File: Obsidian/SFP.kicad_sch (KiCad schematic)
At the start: 41 parts, among them J1 TYCO_1888247-1, J12 TYCO_1888247-1, J8 2180739-1, U17 TCA9555RTWR, U26 PCA9546ARGV

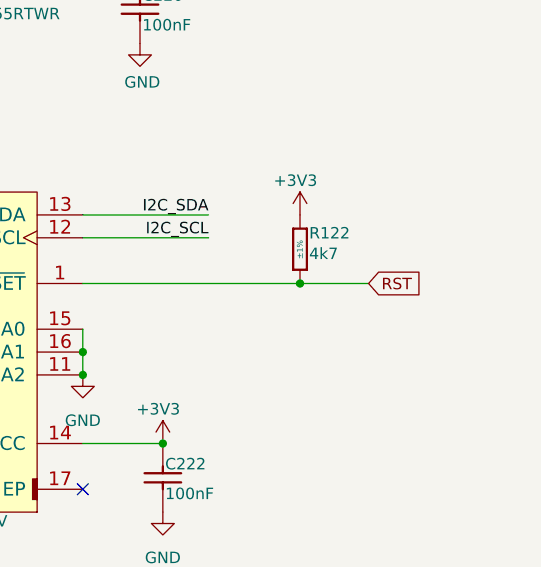
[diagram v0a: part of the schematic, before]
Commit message: removing reset global label
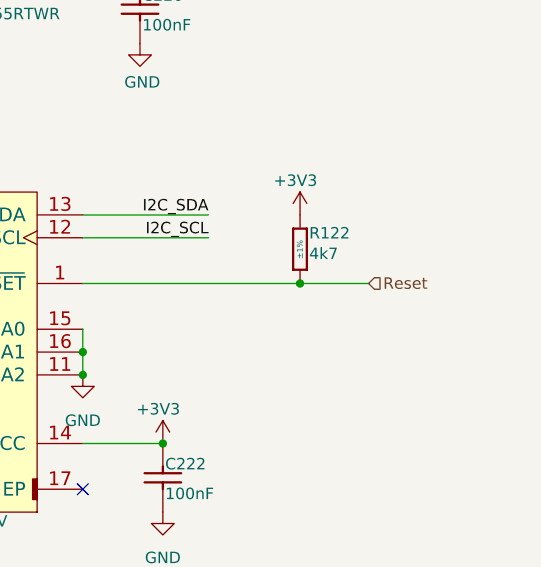
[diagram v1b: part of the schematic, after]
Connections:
- net RST renamed Reset
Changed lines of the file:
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@@
 		)
 	)
-	(global_label "RST"
+	(hierarchical_label "Reset"
 		(shape input)
 		(at 378.46 111.76 0)
-		(fields_autoplaced yes)
 		(effects
 			(font
@@
 			(justify left)
 		)
-		(property "Intersheetrefs" "${INTERSHEET_REFS}"
-			(at 384.8923 111.76 0)
-			(effects
-				(font
-					(size 1.27 1.27)
-				)
-				(justify left)
-				(hide yes)
-			)
-		)
 	)

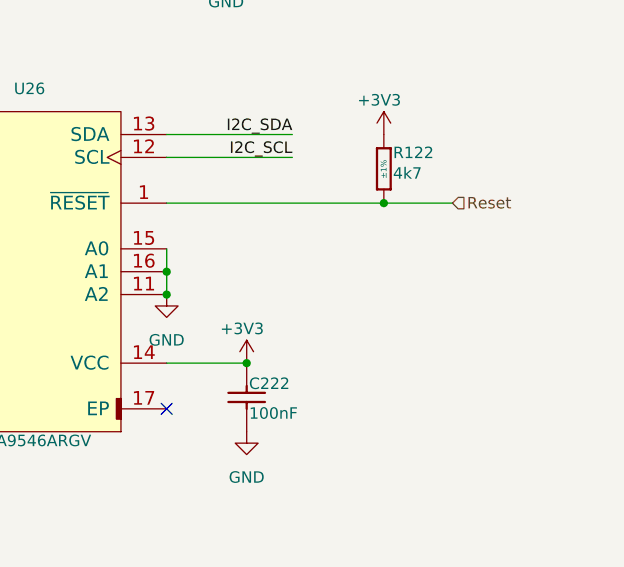
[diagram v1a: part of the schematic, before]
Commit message: adding lcsc reference for PMOD
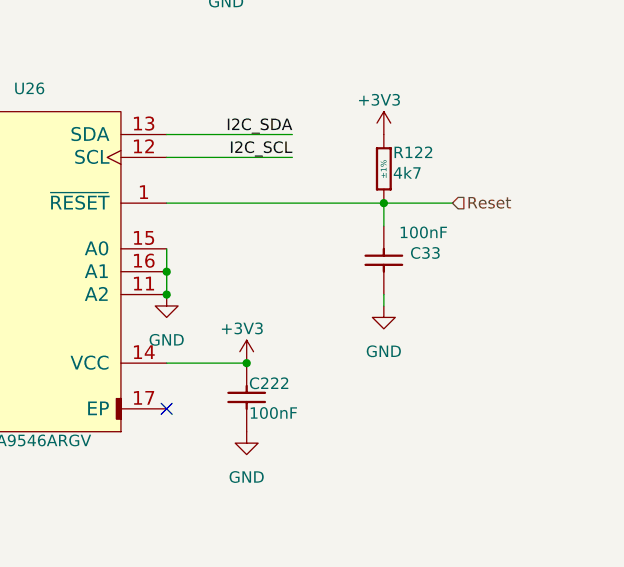
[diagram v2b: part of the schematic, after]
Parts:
- added C33: CC0402_100NF_50V_10%_X7R, Capacitor_SMD:C_0402_1005Metric, symbol Library_Symbol:CC0402_100NF_50V_10%_X7R
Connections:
- net GND: now also C33.2
- net Reset: now also C33.1

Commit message: update LCSC reference, and OFFSET rotation for JLCPCB
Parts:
- C20, C21, C22, C220, C222, C24, C25, C26, C29, C30, C33: footprint Capacitor_SMD:C_0402_1005Metric -> Footprint:CAPC1005X55N
- J1, J12: FT Rotation Offset (none) -> 270
- J8: LCSC C42931391 -> C19267508
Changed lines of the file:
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@@
 			)
 		)
-		(property "Footprint" "Capacitor_SMD:C_0402_1005Metric"
+		(property "Footprint" "Footprint:CAPC1005X55N"
 			(at 145.288 120.65 0)
 			(effects
@@
 			)
 		)
-		(property "Footprint" "Capacitor_SMD:C_0402_1005Metric"
+		(property "Footprint" "Footprint:CAPC1005X55N"
 			(at 145.288 95.25 0)
 			(effects
@@
 			)
 		)
-		(property "Footprint" "Capacitor_SMD:C_0402_1005Metric"
+		(property "Footprint" "Footprint:CAPC1005X55N"
 			(at 121.158 95.25 0)
 			(effects
@@
 			)
 		)
-		(property "Footprint" "Capacitor_SMD:C_0402_1005Metric"
+		(property "Footprint" "Footprint:CAPC1005X55N"
 			(at 145.288 58.42 0)
 			(effects
@@
 			)
 		)
-		(property "FT Rotation Offset" ""
+		(property "FT Rotation Offset" "270"
 			(at 152.4 85.09 0)
 			(effects
@@
 			)
 		)
-		(property "Footprint" "Capacitor_SMD:C_0402_1005Metric"
+		(property "Footprint" "Footprint:CAPC1005X55N"
 			(at 145.288 33.02 0)
 			(effects
@@
 			)
 		)
-		(property "LCSC" "C42931391"
+		(property "LCSC" " C19267508"
 			(at 49.53 35.56 0)
 			(effects
@@
 			)
 		)
-		(property "Footprint" "Capacitor_SMD:C_0402_1005Metric"
+		(property "Footprint" "Footprint:CAPC1005X55N"
 			(at 363.728 137.16 0)
 			(effects
@@
 			)
 		)
-		(property "Footprint" "Capacitor_SMD:C_0402_1005Metric"
+		(property "Footprint" "Footprint:CAPC1005X55N"
 			(at 121.158 33.02 0)
 			(effects
@@
 			)
 		)
-		(property "Footprint" "Capacitor_SMD:C_0402_1005Metric"
+		(property "Footprint" "Footprint:CAPC1005X55N"
 			(at 362.712 114.3 0)
 			(effects
@@
 			)
 		)
-		(property "Footprint" "Capacitor_SMD:C_0402_1005Metric"
+		(property "Footprint" "Footprint:CAPC1005X55N"
 			(at 121.158 58.42 0)
 			(effects
@@
 			)
 		)
-		(property "FT Rotation Offset" ""
+		(property "FT Rotation Offset" "270"
 			(at 152.4 22.86 0)
 			(effects
@@
 			)
 		)
-		(property "Footprint" "Capacitor_SMD:C_0402_1005Metric"
+		(property "Footprint" "Footprint:CAPC1005X55N"
 			(at 121.158 120.65 0)
 			(effects
@@
 			)
 		)
-		(property "Footprint" "Capacitor_SMD:C_0402_1005Metric"
+		(property "Footprint" "Footprint:CAPC1005X55N"
 			(at 361.188 85.09 0)
 			(effects

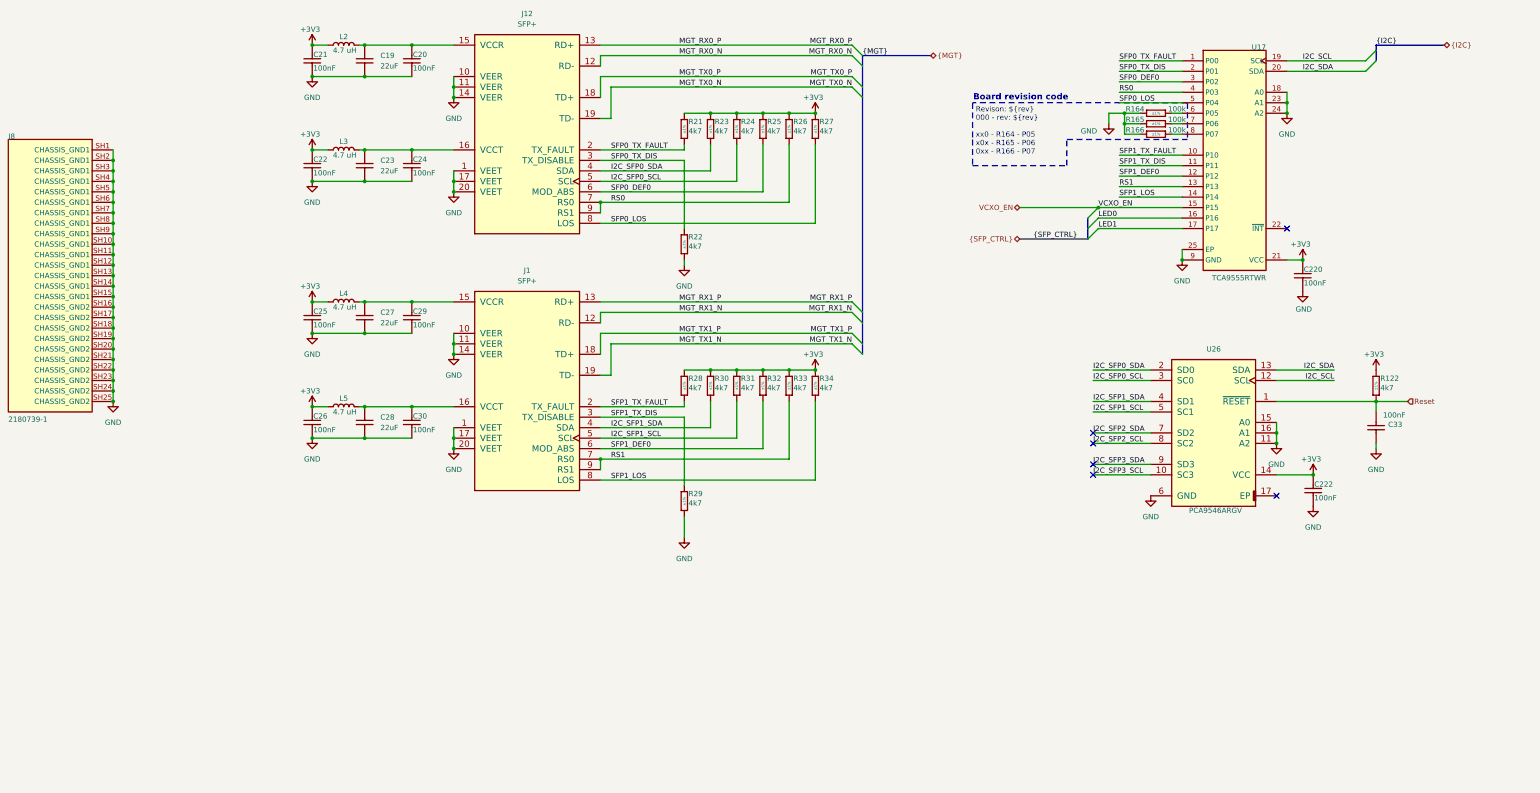
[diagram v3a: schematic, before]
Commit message: Adding documentation for configuration with flash memory, adding more comments to schematic
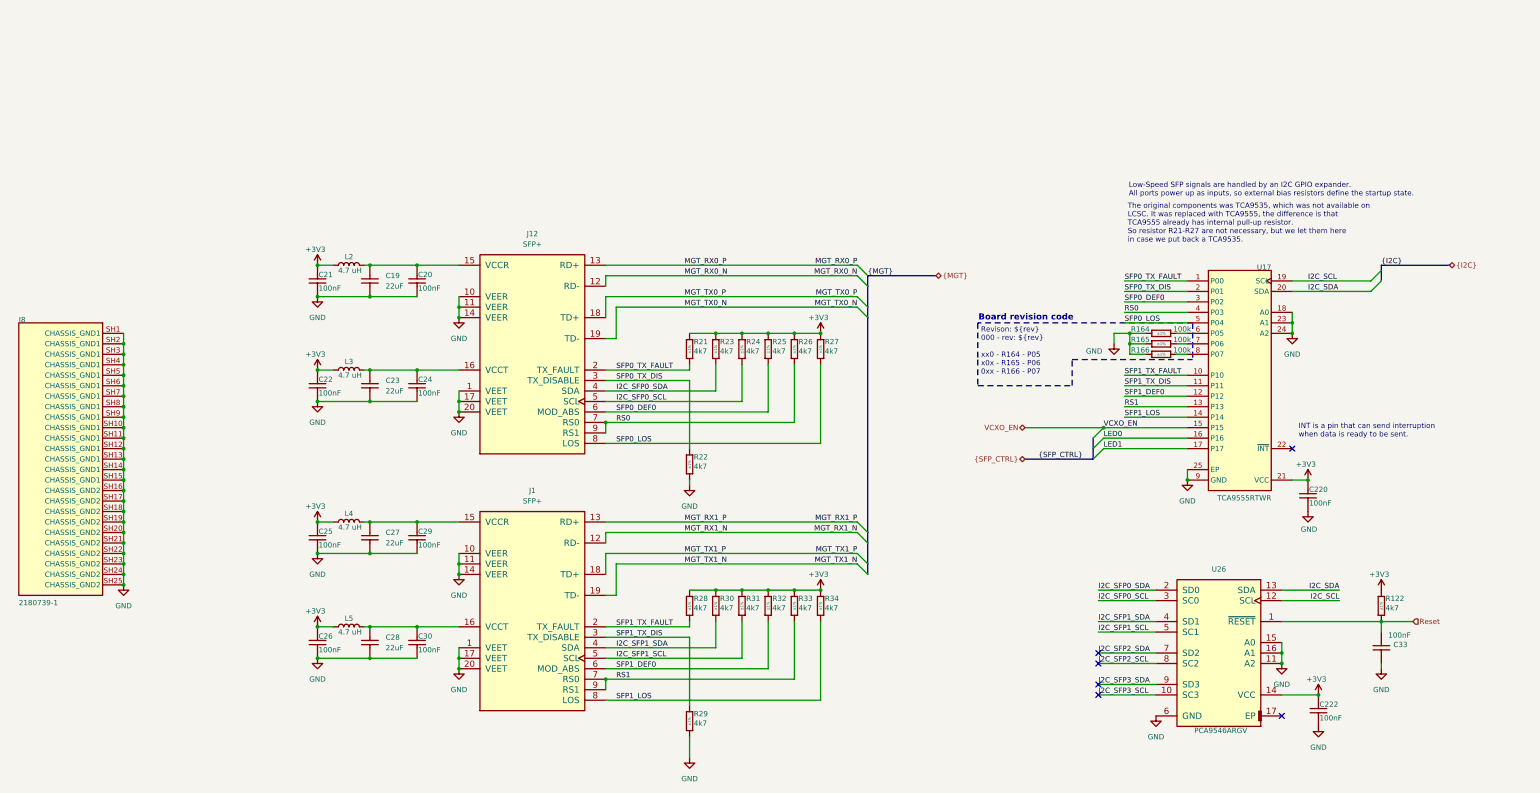
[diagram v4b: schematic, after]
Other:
- note added: "INT is a pin that can send interruption when data is ready to be sent."
- note added: "Low-Speed SFP signals are handled by an I2C GPIO expander. All ports power up as inputs, so external bias resistors define the startup state."
- note added: "The original components was TCA9535, which was not available on LCSC. It was replaced with TCA9555, the difference is that TCA9555 already has internal pull-up resistor. So resistor R21-R27 are not necessary, but we let them here in case we put back a TCA9535."
- moved on the sheet: C19, C20, C21, C22, C220, C222, C23, C24, C25, C26, C27, C28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

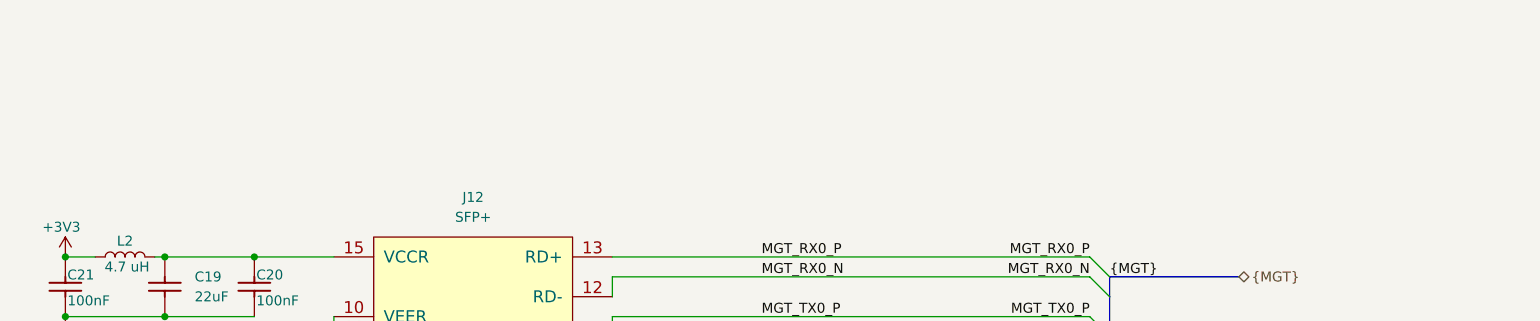
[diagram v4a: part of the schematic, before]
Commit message: adding comments, and test point for U12 (power supply in clock sheet)
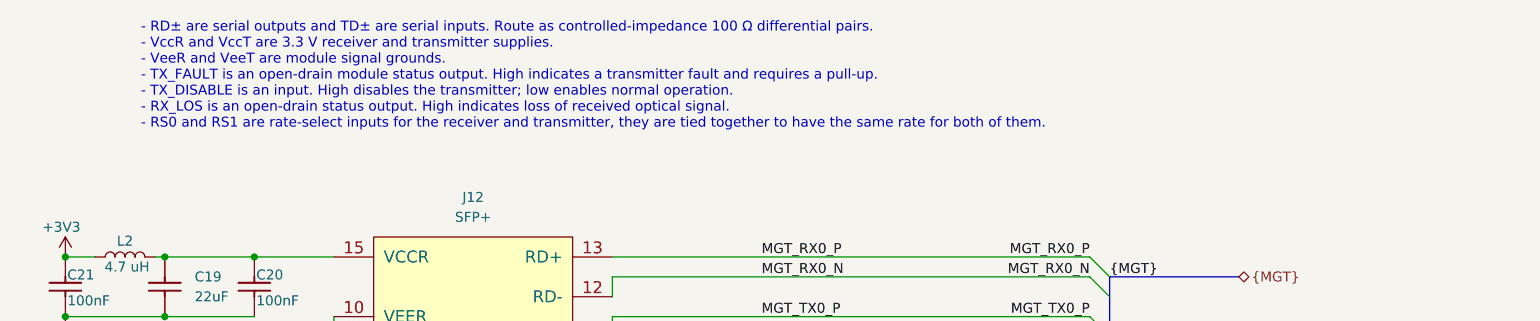
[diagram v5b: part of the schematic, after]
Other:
- note added: "- RD± are serial outputs and TD± are serial inputs. Route as controlled-impedance 100 Ω differential pairs. - VccR and VccT are 3.3 V receiver and transmitter supplies. - VeeR and VeeT are module signal grounds. - TX_FAULT is an open-drain module status output. High indicates a transmitter fault and requires a pull-up. - TX_DISABLE is an input. High disables the transmitter; low enables normal op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"
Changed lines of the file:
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@@
+		)
+	)
+	(text "- RD± are serial outputs and TD± are serial inputs. Route as controlled-impedance 100 Ω differential pairs.\n- VccR and VccT are 3.3 V receiver and transmitter supplies.\n- VeeR and VeeT are module signal grounds.\n- TX_FAULT is an open-drain module status output. High indicates a transmitter fault and requires a pull-up.\n- TX_DISABLE is an input. High disables the transmitter; low enables normal operation.\n- RX_LOS is an open-drain status output. High indicates loss of received optical signal.\n- RS0 and RS1 are rate-select inputs for the receiver and transmitter, they are tied together to have the same rate for both of them."
+		(exclude_from_sim no)
+		(at 123.952 55.626 0)
+		(effects
+			(font
+				(size 1.27 1.27)
+			)
+			(justify left)
 		)
 	)

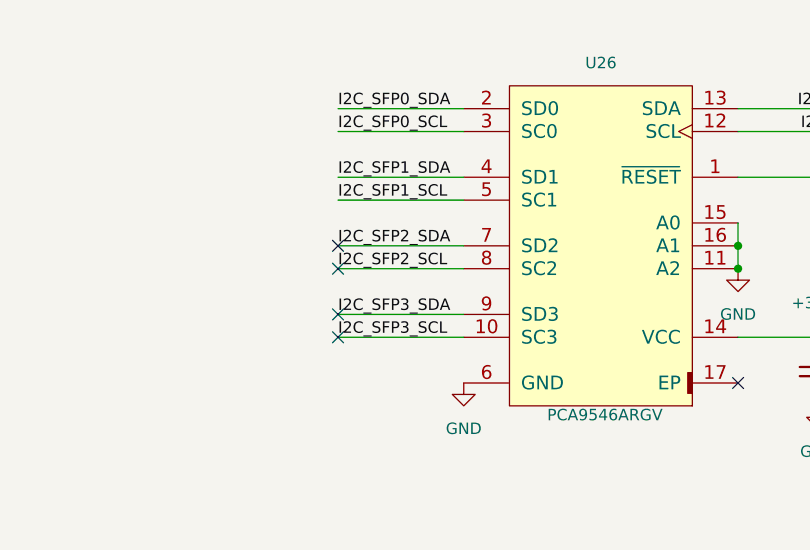
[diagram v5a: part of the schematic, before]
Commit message: Putting back S25FL128SAGMFI001 in FPGA_DBG sheet, see #17
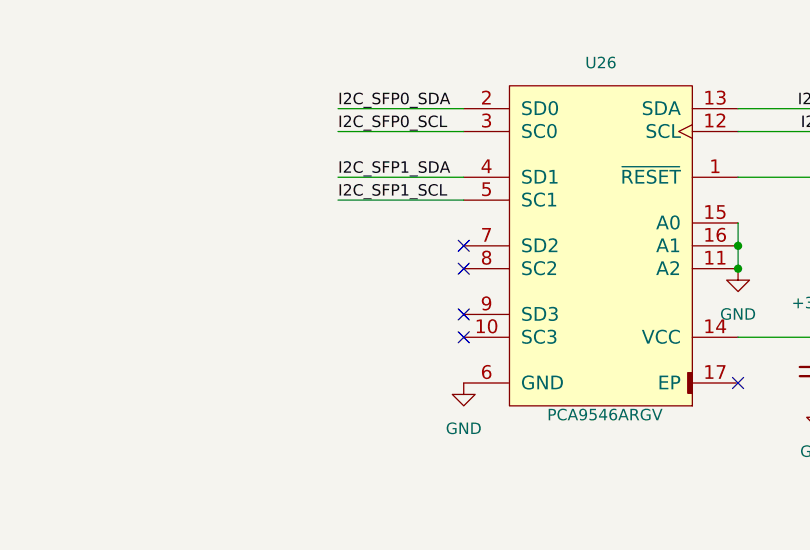
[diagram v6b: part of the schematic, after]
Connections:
- net I2C_SFP2_SCL: no longer names the net of U26.8 (SC2)
- net I2C_SFP2_SDA: no longer names the net of U26.7 (SD2)
- net I2C_SFP3_SCL: no longer names the net of U26.10 (SC3)
- net I2C_SFP3_SDA: no longer names the net of U26.9 (SD3)
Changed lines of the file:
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@@
 	)
 	(no_connect
-		(at 303.53 182.88)
+		(at 317.5 182.88)
 	)
 	(no_connect
@@
 	)
 	(no_connect
-		(at 303.53 175.26)
+		(at 317.5 175.26)
 	)
 	(no_connect
-		(at 303.53 180.34)
+		(at 317.5 180.34)
 	)
 	(no_connect
-		(at 303.53 172.72)
+		(at 317.5 172.72)
 	)
 	(no_connect
@@
 	(wire
 		(pts
-			(xy 303.53 180.34) (xy 317.5 180.34)
-		)
-		(stroke
-			(width 0)
-			(type default)
-		)
-	)
-	(wire
-		(pts
 			(xy 217.17 157.48) (xy 223.52 157.48)
 		)
@@
 	(wire
 		(pts
-			(xy 303.53 172.72) (xy 317.5 172.72)
-		)
-		(stroke
-			(width 0)
-			(type default)
-		)
-	)
-	(wire
-		(pts
 			(xy 125.73 166.37) (xy 127 166.37)
 		)
@@
 		)
 	)
-	(wire
-		(pts
-			(xy 303.53 175.26) (xy 317.5 175.26)
-		)
-		(stroke
-			(width 0)
-			(type default)
-		)
-	)
 	(polyline
 		(pts
@@
 	(wire
 		(pts
-			(xy 303.53 182.88) (xy 317.5 182.88)
-		)
-		(stroke
-			(width 0)
-			(type default)
-		)
-	)
-	(wire
-		(pts
 			(xy 148.59 171.45) (xy 148.59 173.99)
 		)
@@
 			(width 0)
 			(type default)
-		)
-	)
-	(label "I2C_SFP2_SCL"
-		(at 303.53 175.26 0)
-		(effects
-			(font
-				(size 1.27 1.27)
-				(thickness 0.1588)
-			)
-			(justify left bottom)
 		)
 	)
@@
 		)
 	)
-	(label "I2C_SFP2_SDA"
-		(at 303.53 172.72 0)
-		(effects
-			(font
-				(size 1.27 1.27)
-				(thickness 0.1588)
-			)
-			(justify left bottom)
-		)
-	)
 	(label "LED0"
 		(at 304.8 120.65 0)
@@
 		)
 	)
-	(label "I2C_SFP3_SDA"
-		(at 303.53 180.34 0)
-		(effects
-			(font
-				(size 1.27 1.27)
-				(thickness 0.1588)
-			)
-			(justify left bottom)
-		)
-	)
 	(label "SFP1_LOS"
 		(at 186.69 184.15 0)
@@
 			)
 			(justify left bottom)
-		)
-	)
-	(label "I2C_SFP3_SCL"
-		(at 303.53 182.88 0)
-		(effects
-			(font
-				(size 1.27 1.27)
-				(thickness 0.1588)
-			)
-			(justify left bottom)

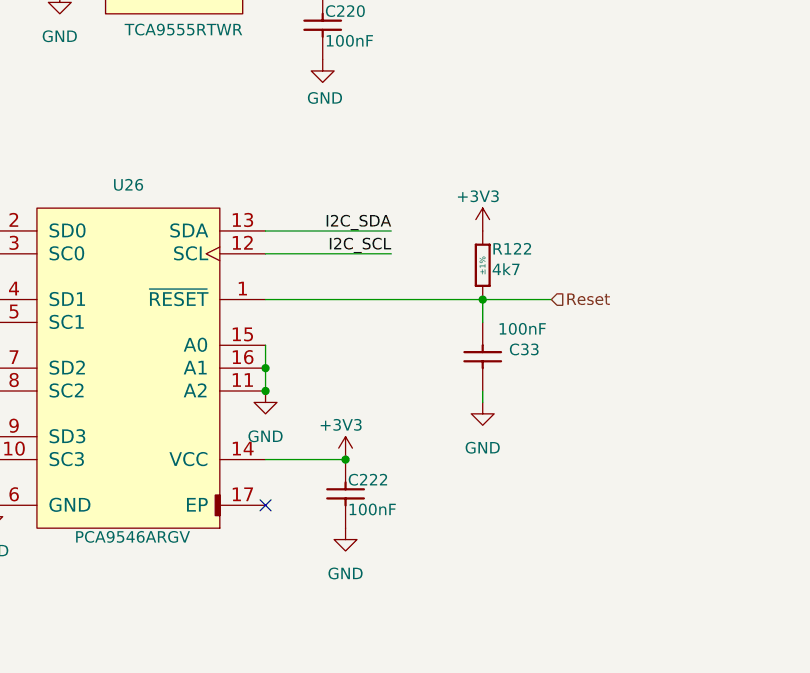
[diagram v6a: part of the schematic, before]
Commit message: Update TPSM863257RDXR symbol to set output pins as output power. Putting pull-up resistor on flash spi, decoupling capacitor and deconnect Vio.
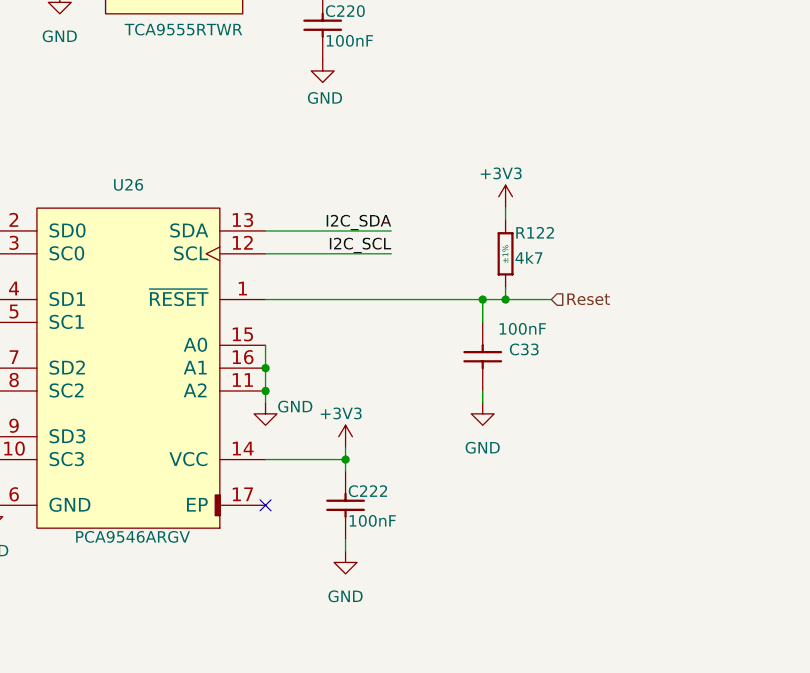
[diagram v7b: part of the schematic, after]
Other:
- moved on the sheet: C222, R122
